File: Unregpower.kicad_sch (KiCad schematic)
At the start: 13 parts

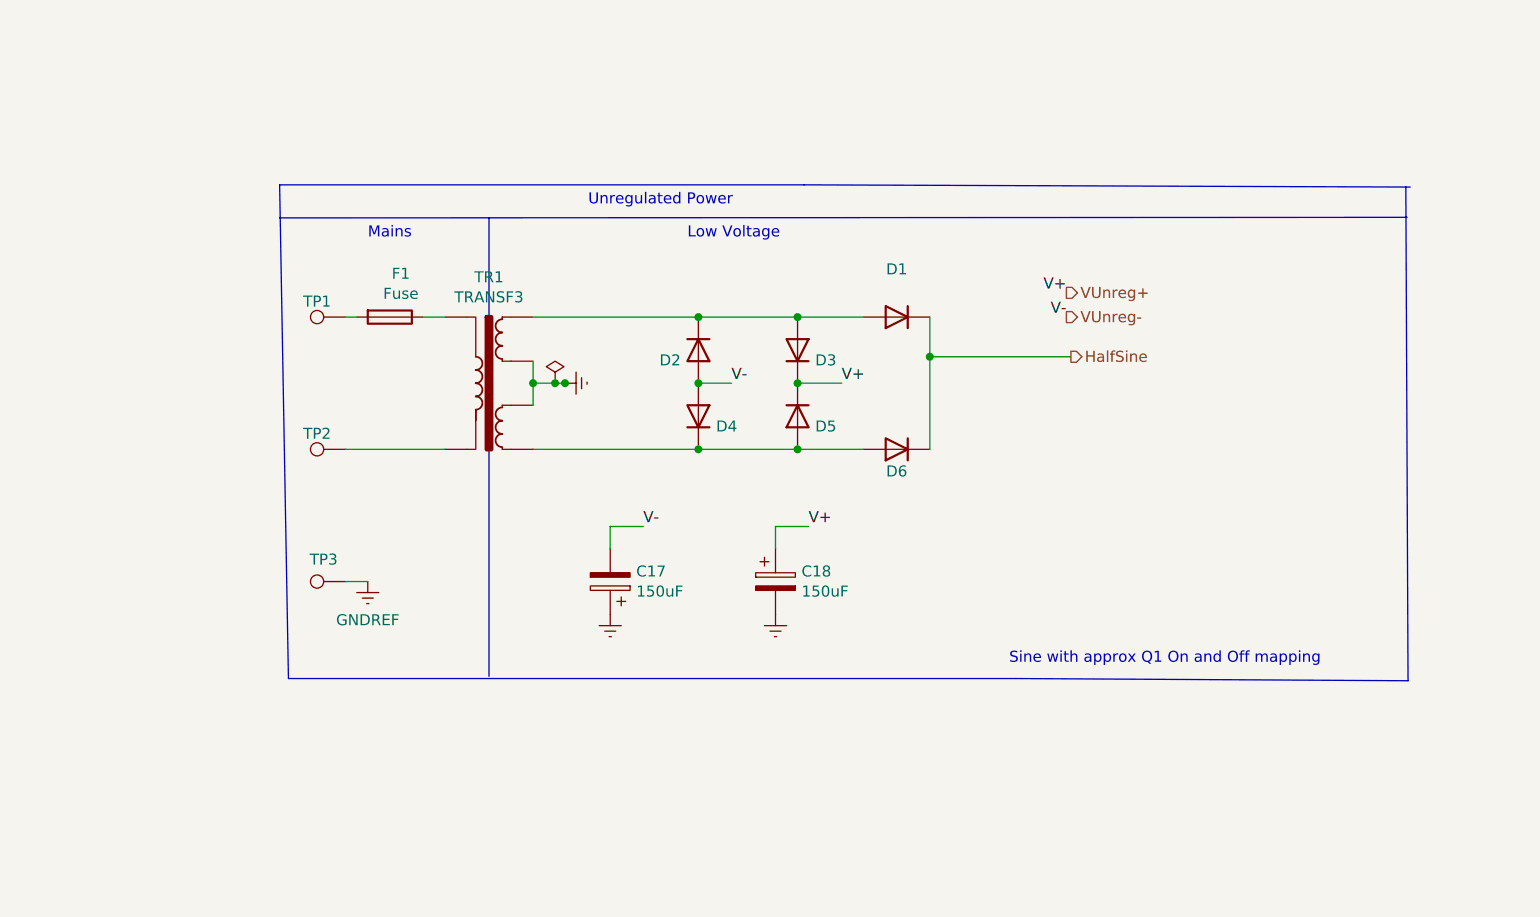
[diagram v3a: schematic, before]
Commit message: Updated improved board for all SMD
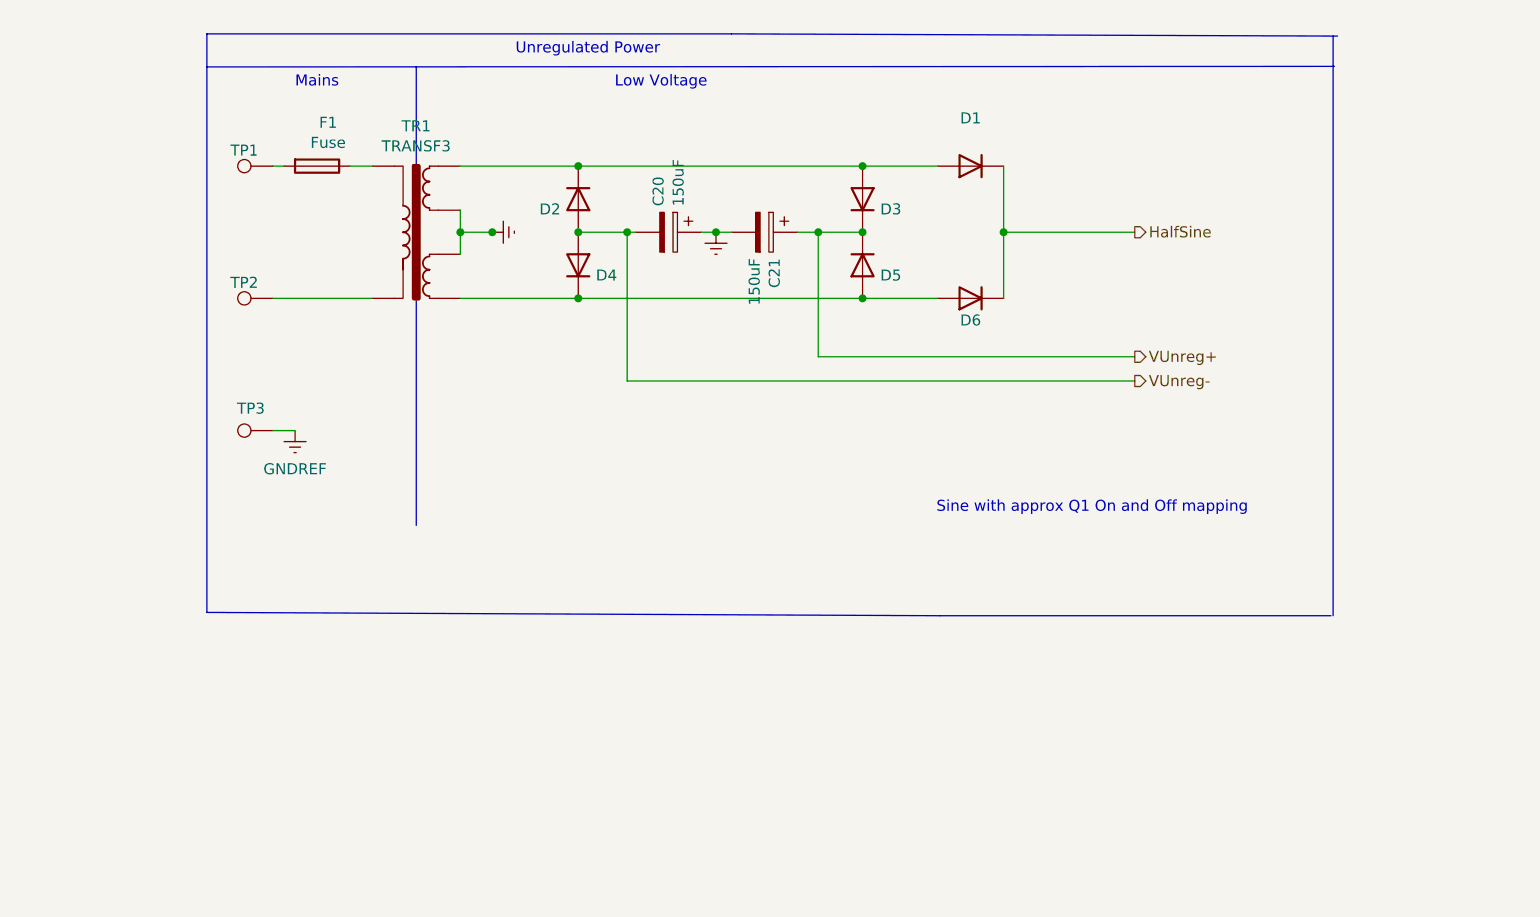
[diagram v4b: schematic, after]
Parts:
- renumbered C17 to C20, C18 to C21
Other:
- moved on the sheet: C20, C21, D1, D2, D3, D4, D5, D6, F1, TP1, TP2, TP3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

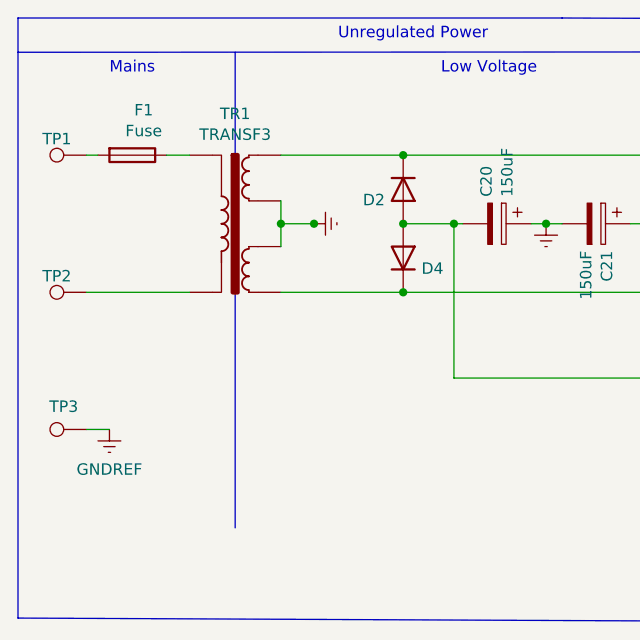
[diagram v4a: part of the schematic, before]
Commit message: Refined board and kerned size down
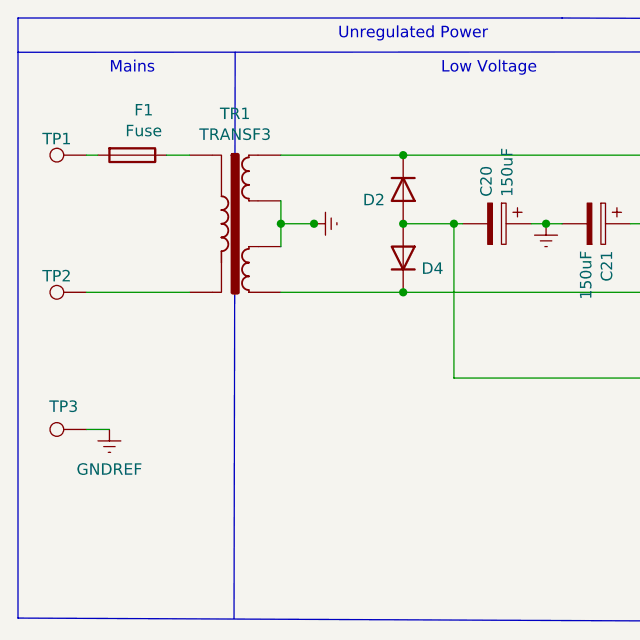
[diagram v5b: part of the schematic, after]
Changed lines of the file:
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@@
     (stroke (width 0) (type default) (color 0 0 0 0))
   )
-  (polyline (pts (xy 101.346 66.675) (xy 101.346 119.507))
+  (polyline (pts (xy 101.346 66.675) (xy 101.219 129.54))
     (stroke (width 0) (type default) (color 0 0 0 0))
   )
@@
     (stroke (width 0) (type default) (color 0 0 0 0))
   )
-  (image (at 131.064 108.585) (scale 0.612075)
+  (image (at 128.143 114.2492) (scale 0.612075)
     (data
       iVBORw0KGgoAAAANSUhEUgAAA40AAAIhCAIAAABln8hPAAAAA3NCSVQICAjb4U/gAAAACXBIWXMA

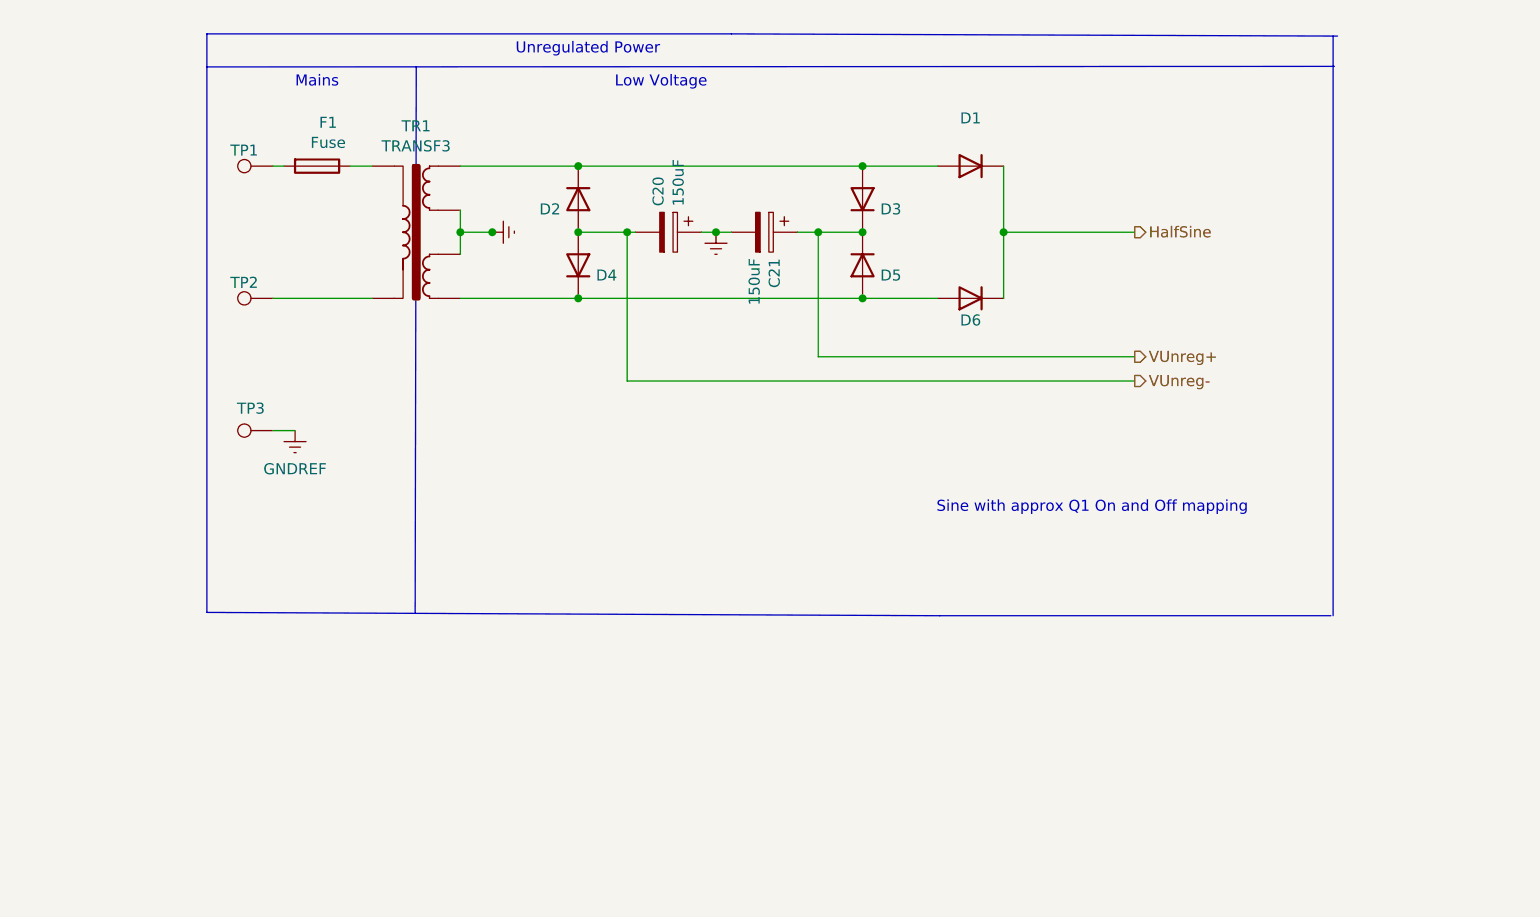
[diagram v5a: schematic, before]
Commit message: added new op amps and used automated traces due to complexity
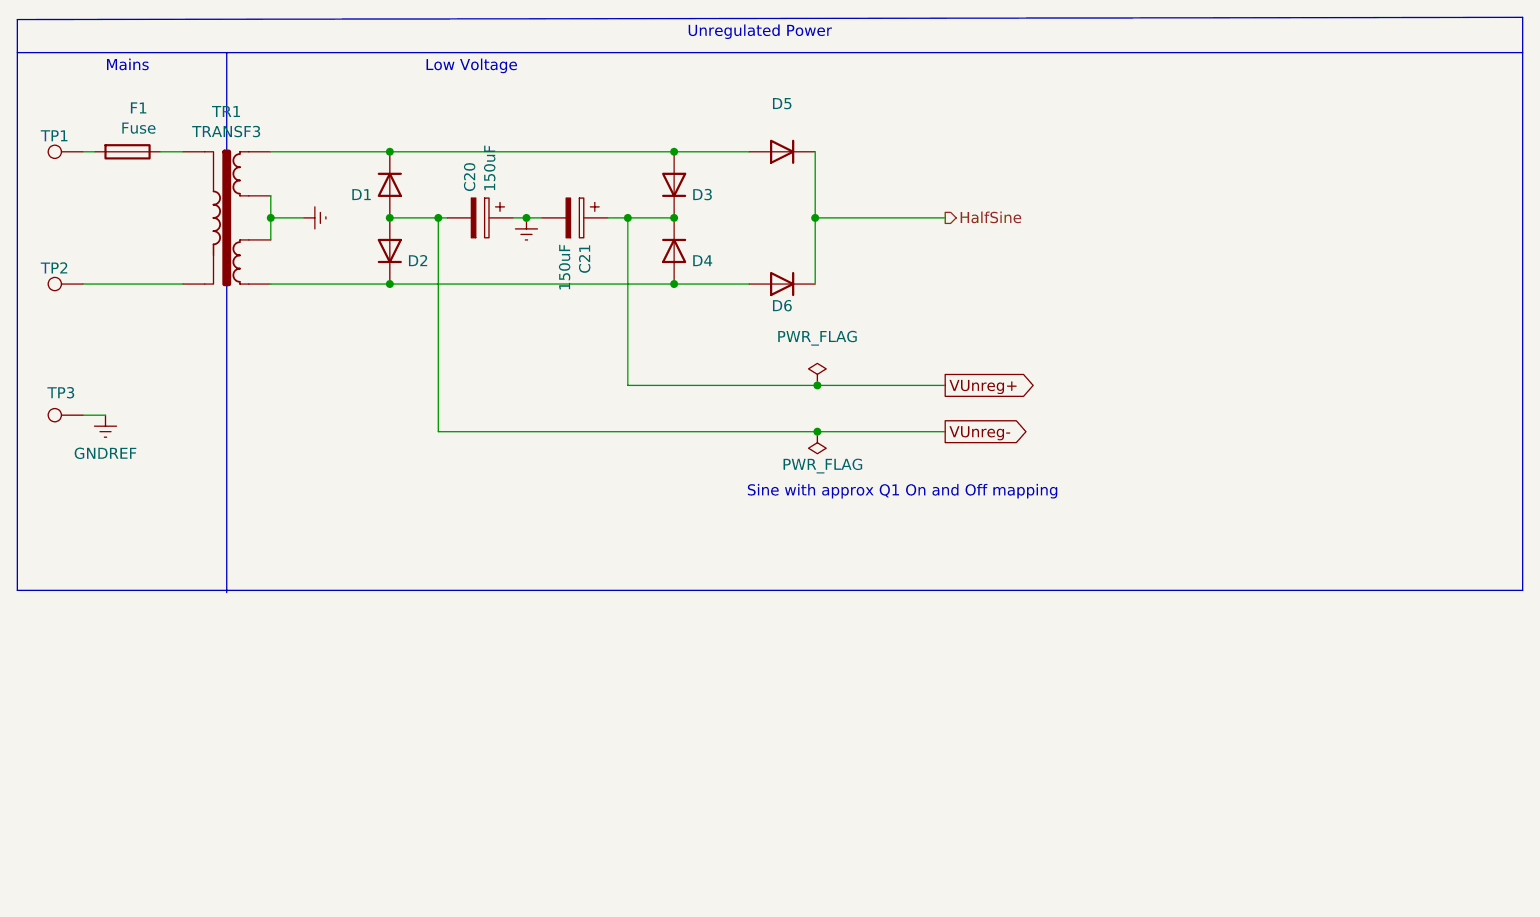
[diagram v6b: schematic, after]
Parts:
- renumbered D2 to D1, D4 to D2, D5 to D4, D1 to D5
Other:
- moved on the sheet: C20, C21, D1, D2, D3, D4, D5, D6, F1, TP1, TP2, TP3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

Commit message: new EMC-EMI layout with improved suppression
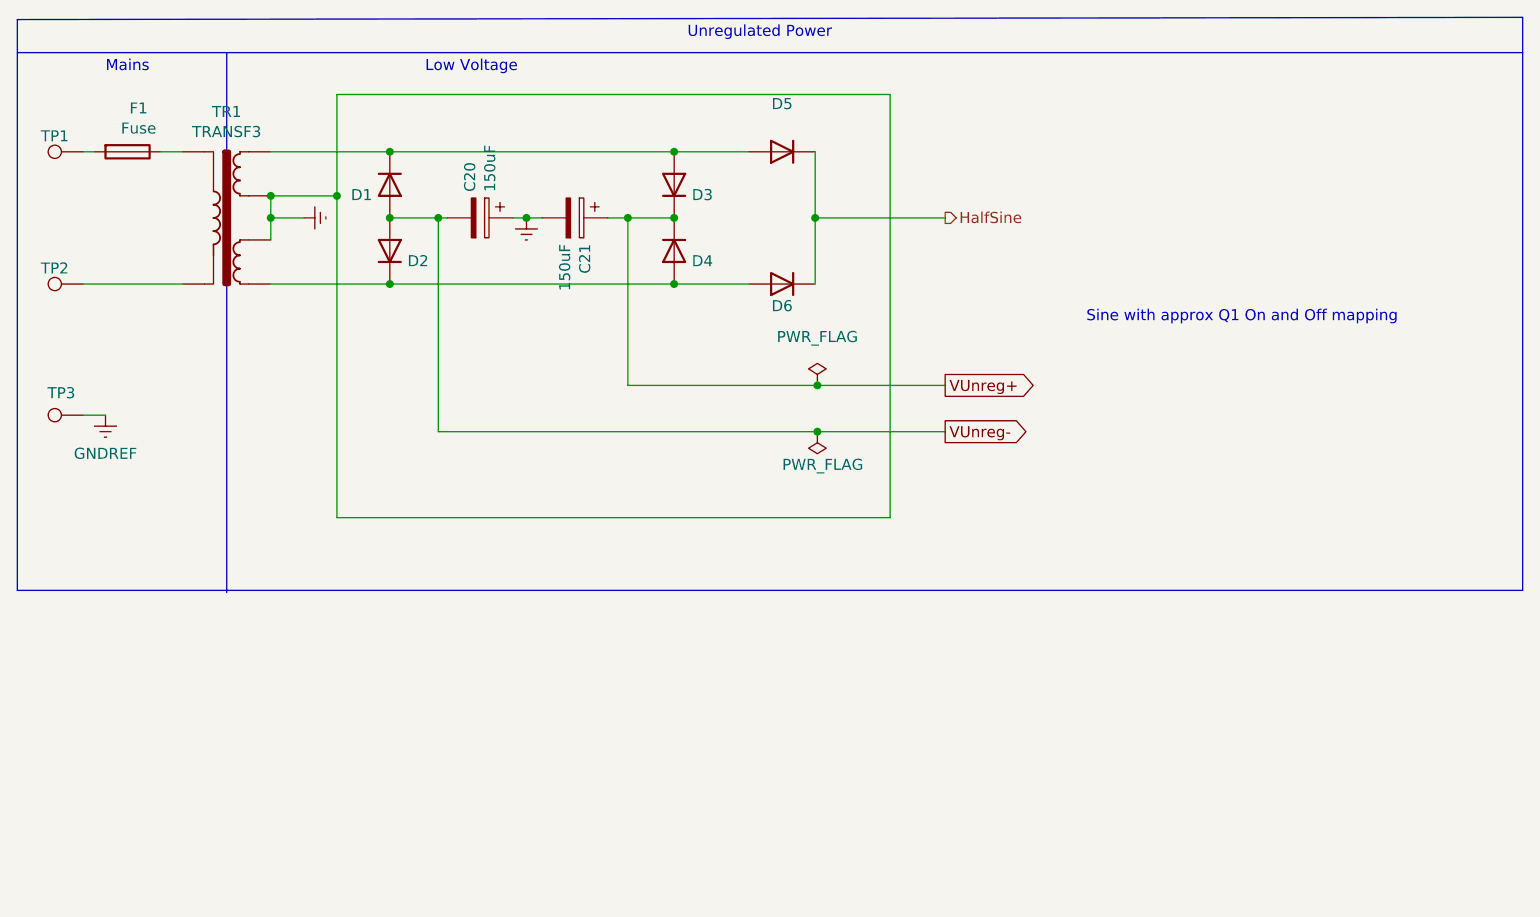
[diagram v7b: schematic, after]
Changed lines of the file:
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@@
 (kicad_sch (version 20211123) (generator eeschema)
   (paper "A4")
+  (junction (at 92.202 81.534) (diameter 0) (color 0 0 0 0)
+  )
   (junction (at 131.064 76.454) (diameter 0) (color 0 0 0 0)
   )
   (junction (at 147.574 103.378) (diameter 0) (color 0 0 0 0)
   )
+  (junction (at 84.582 81.534) (diameter 0) (color 0 0 0 0)
+  )
   (junction (at 84.582 84.074) (diameter 0) (color 0 0 0 0)
   )
@@
     (stroke (width 0) (type default) (color 0 0 0 0))
   )
+  (wire (pts (xy 92.202 81.534) (xy 92.202 118.618))
+    (stroke (width 0) (type default) (color 0 0 0 0))
+  )
   (wire (pts (xy 125.73 84.074) (xy 131.064 84.074))
     (stroke (width 0) (type default) (color 0 0 0 0))
@@
     (stroke (width 0) (type default) (color 0 0 0 0))
   )
+  (wire (pts (xy 84.582 81.534) (xy 92.202 81.534))
+    (stroke (width 0) (type default) (color 0 0 0 0))
+  )
   (polyline (pts (xy 228.854 127) (xy 228.854 60.96))
     (stroke (width 0) (type default) (color 0 0 0 0))
   )
+  (wire (pts (xy 155.956 69.85) (xy 155.956 118.618))
+    (stroke (width 0) (type default) (color 0 0 0 0))
+  )
+  (wire (pts (xy 92.202 69.85) (xy 92.202 81.534))
+    (stroke (width 0) (type default) (color 0 0 0 0))
+  )
   (wire (pts (xy 71.882 76.454) (xy 74.422 76.454))
     (stroke (width 0) (type default) (color 0 0 0 0))
   )
-  (wire (pts (xy 147.574 103.378) (xy 125.73 103.378))
+  (wire (pts (xy 103.886 108.712) (xy 147.574 108.712))
+    (stroke (width 0) (type default) (color 0 0 0 0))
+  )
+  (wire (pts (xy 125.73 103.378) (xy 147.574 103.378))
     (stroke (width 0) (type default) (color 0 0 0 0))
   )
@@
     (stroke (width 0) (type default) (color 0 0 0 0))
   )
+  (wire (pts (xy 92.202 69.85) (xy 155.956 69.85))
+    (stroke (width 0) (type default) (color 0 0 0 0))
+  )
   (wire (pts (xy 84.582 84.074) (xy 84.582 86.614))
     (stroke (width 0) (type default) (color 0 0 0 0))
@@
     (stroke (width 0) (type default) (color 0 0 0 0))
   )
+  (wire (pts (xy 155.956 118.618) (xy 92.202 118.618))
+    (stroke (width 0) (type default) (color 0 0 0 0))
+  )
   (wire (pts (xy 84.582 76.454) (xy 98.298 76.454))
     (stroke (width 0) (type default) (color 0 0 0 0))
@@
   )
   (wire (pts (xy 103.886 84.074) (xy 103.886 108.712))
-    (stroke (width 0) (type default) (color 0 0 0 0))
-  )
-  (wire (pts (xy 147.574 108.712) (xy 103.886 108.712))
     (stroke (width 0) (type default) (color 0 0 0 0))
   )
@@
     (effects (font (size 1.27 1.27)) (justify left bottom))
   )
-  (text "Sine with approx Q1 On and Off mapping" (at 139.446 116.459 0)
+  (text "Sine with approx Q1 On and Off mapping" (at 178.562 96.266 0)
     (effects (font (size 1.27 1.27)) (justify left bottom))
   )

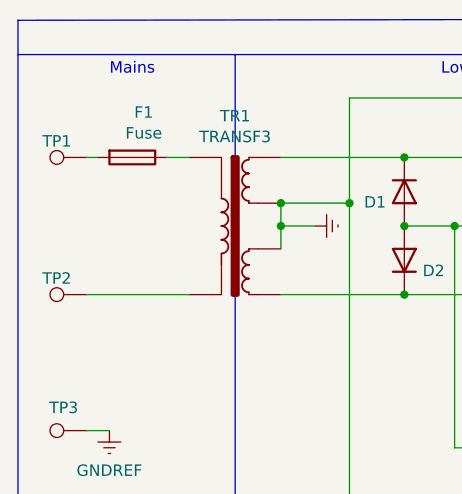
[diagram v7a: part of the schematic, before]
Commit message: updated with extra filtering and guard ring placement
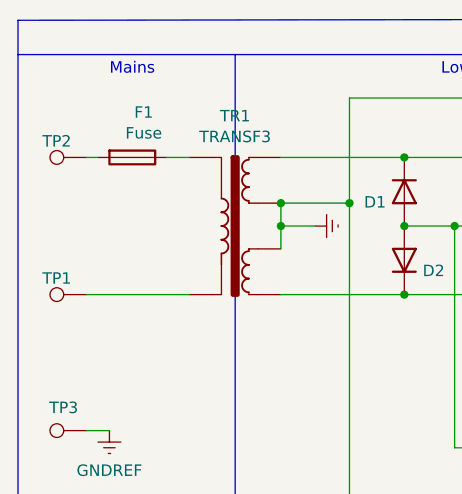
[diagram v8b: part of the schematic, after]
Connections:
- net at TP2.1: now also F1.2; no longer TR1.2
- net at TP1.1: now also TR1.2; no longer F1.2
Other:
- moved on the sheet: TP1, TP2
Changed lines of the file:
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@@
     (effects (font (size 1.27 1.27)) (justify left))
   )
-  (symbol (lib_id "Connector:TestPoint") (at 62.992 91.694 90) (unit 1)
+  (symbol (lib_id "Connector:TestPoint") (at 62.992 76.454 90) (unit 1)
     (in_bom yes) (on_board yes) (fields_autoplaced)
-    (property "Reference" "TP2" (id 0) (at 59.69 89.8962 90))
-    (property "Value" "TestPoint" (id 1) (at 59.69 89.8961 90)
+    (property "Reference" "TP2" (id 0) (at 59.69 74.6562 90))
+    (property "Value" "TestPoint" (id 1) (at 59.69 74.6561 90)
       (effects (font (size 1.27 1.27)) hide)
     )
-    (property "Footprint" "TestPoint:TestPoint_THTPad_4.0x4.0mm_Drill2.0mm" (id 2) (at 62.992 86.614 0)
+    (property "Footprint" "TestPoint:TestPoint_THTPad_4.0x4.0mm_Drill2.0mm" (id 2) (at 62.992 71.374 0)
       (effects (font (size 1.27 1.27)) hide)
     )
-    (property "Datasheet" "~" (id 3) (at 62.992 86.614 0)
+    (property "Datasheet" "~" (id 3) (at 62.992 71.374 0)
       (effects (font (size 1.27 1.27)) hide)
     )
@@
     (pin "2")
   )
-  (symbol (lib_id "Connector:TestPoint") (at 62.992 76.454 90) (unit 1)
+  (symbol (lib_id "Connector:TestPoint") (at 62.992 91.694 90) (unit 1)
     (in_bom yes) (on_board yes) (fields_autoplaced)
-    (property "Reference" "TP1" (id 0) (at 59.69 74.6562 90))
-    (property "Value" "TestPoint" (id 1) (at 59.69 74.6561 90)
+    (property "Reference" "TP1" (id 0) (at 59.69 89.8962 90))
+    (property "Value" "TestPoint" (id 1) (at 59.69 89.8961 90)
       (effects (font (size 1.27 1.27)) hide)
     )
-    (property "Footprint" "TestPoint:TestPoint_THTPad_4.0x4.0mm_Drill2.0mm" (id 2) (at 62.992 71.374 0)
+    (property "Footprint" "TestPoint:TestPoint_THTPad_4.0x4.0mm_Drill2.0mm" (id 2) (at 62.992 86.614 0)
       (effects (font (size 1.27 1.27)) hide)
     )
-    (property "Datasheet" "~" (id 3) (at 62.992 71.374 0)
+    (property "Datasheet" "~" (id 3) (at 62.992 86.614 0)
       (effects (font (size 1.27 1.27)) hide)
     )
